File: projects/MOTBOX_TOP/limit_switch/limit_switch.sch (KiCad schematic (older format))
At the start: 3 parts, among them J1 Conn_02x02_Top_Bottom, SW1 SW_SPST, SW2 SW_SPST

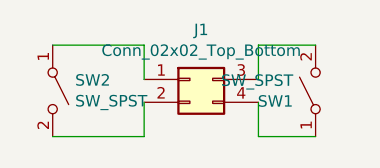
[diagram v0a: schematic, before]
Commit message: New library files and schematics with ESE31 and DT045 switches
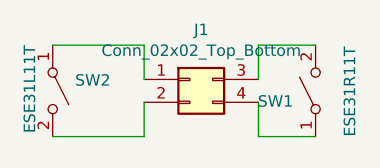
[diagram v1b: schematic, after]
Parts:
- SW1: value SW_SPST -> ESE31R11T; footprint mylib:Detector_SW_2pin_left -> mylib:ESE58R11T_Detector_SW_2pin_right
- SW2: value SW_SPST -> ESE31L11T; footprint mylib:Detector_SW_2pin_right -> mylib:ESE58L11T_Detector_SW_2pin_left
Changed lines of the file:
@@
 P 3050 2800
 F 0 "SW2" V 3004 2898 50  0000 L CNN
-F 1 "SW_SPST" V 3095 2898 50  0000 L CNN
-F 2 "mylib:Detector_SW_2pin_right" H 3050 2800 50  0001 C CNN
+F 1 "ESE31L11T" H 2850 2700 50  0000 L CNN
+F 2 "mylib:ESE58L11T_Detector_SW_2pin_left" H 3050 2800 50  0001 C CNN
 F 3 "" H 3050 2800 50  0001 C CNN
 	1    3050 2800
@@
 P 4200 2800
 F 0 "SW1" V 4154 2898 50  0000 L CNN
-F 1 "SW_SPST" V 4245 2898 50  0000 L CNN
-F 2 "mylib:Detector_SW_2pin_left" H 4200 2800 50  0001 C CNN
+F 1 "ESE31R11T" H 4000 2650 50  0000 L CNN
+F 2 "mylib:ESE58R11T_Detector_SW_2pin_right" H 4200 2800 50  0001 C CNN
 F 3 "" H 4200 2800 50  0001 C CNN
 	1    4200 2800
